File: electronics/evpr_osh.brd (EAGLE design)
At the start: 88.6 x 42.7 mm, 140 parts

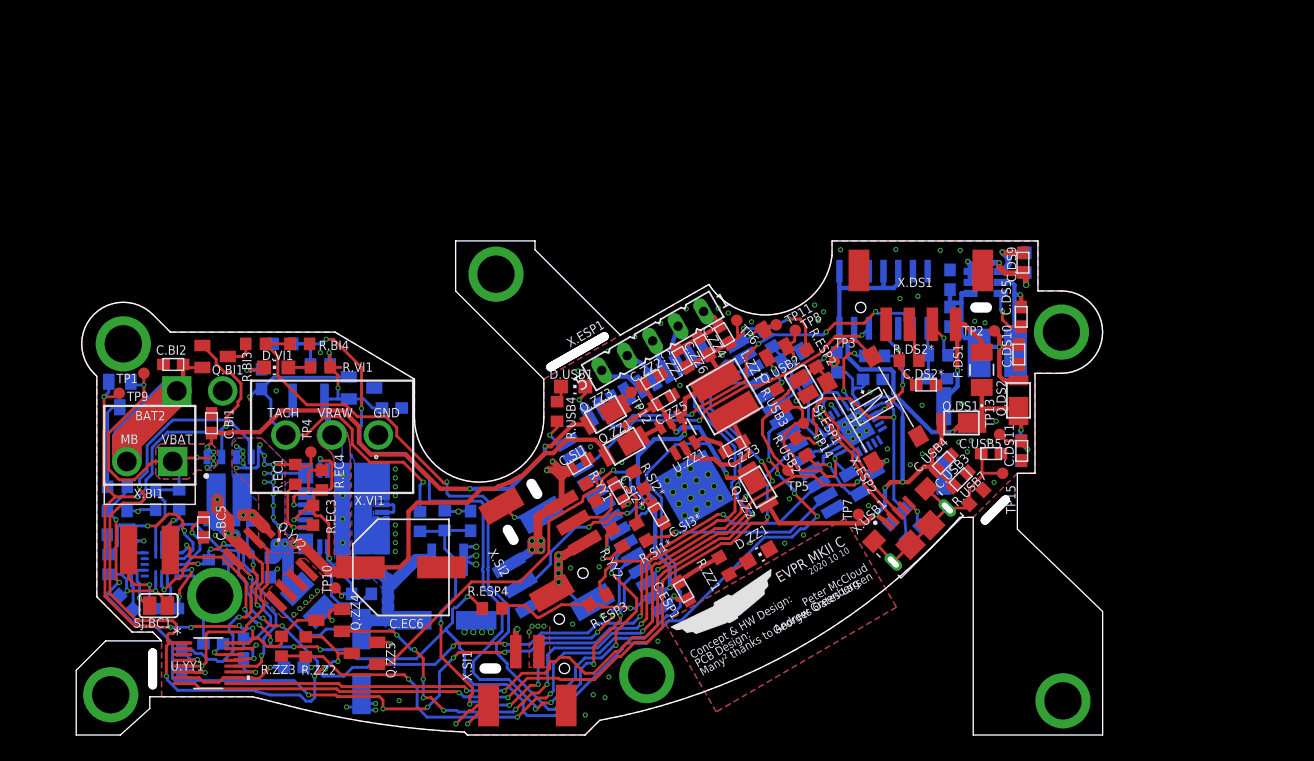
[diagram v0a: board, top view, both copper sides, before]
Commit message: Created OSH version with out-of-board holes removed and shims added. Bumped revision to MKII.D
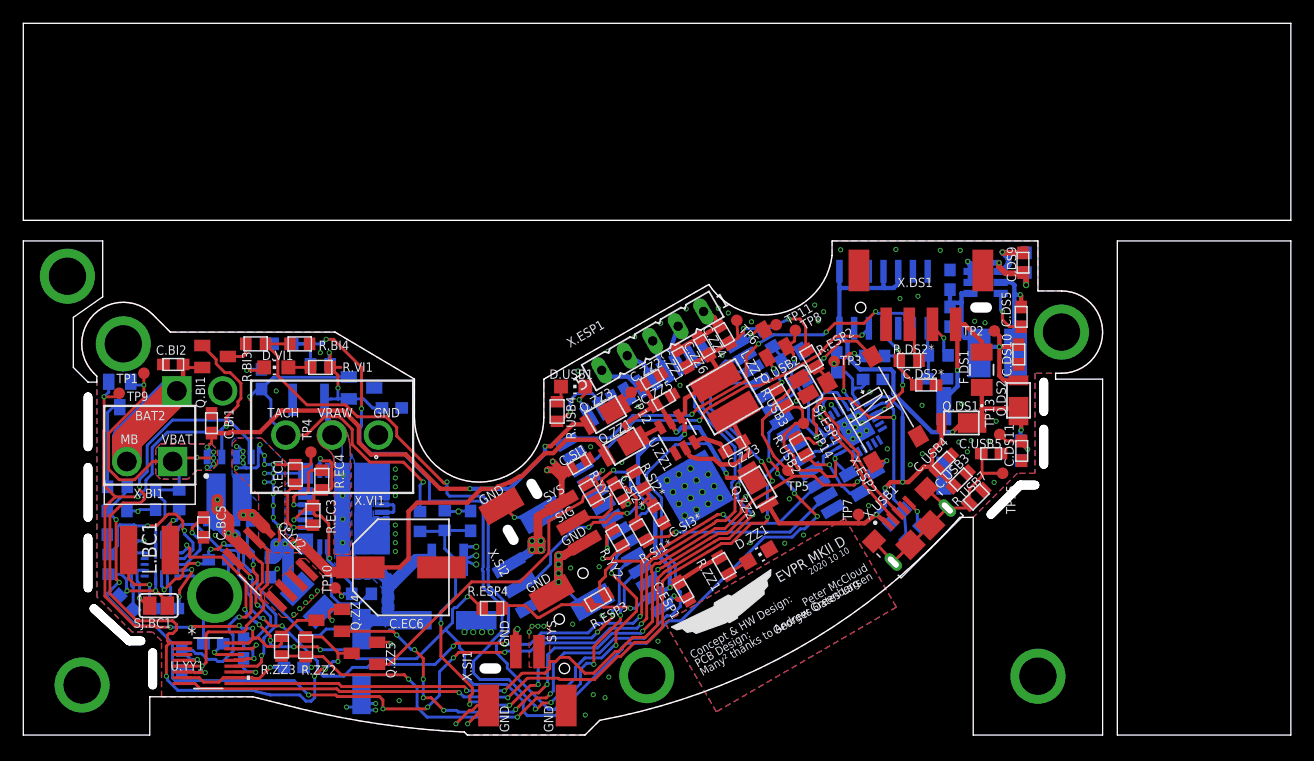
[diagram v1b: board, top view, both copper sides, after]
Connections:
- net USING_ENG renamed !USING_ENG
- new net !USING_BAT: U.ESP1.26
- net DS_CLK: now also U.ESP1.14; no longer U.ESP1.16
- net LED_BUILTIN: now also U.ESP1.16; no longer U.ESP1.14
- net USING_BAT: no longer U.ESP1.26
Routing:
- net LED_BUILTIN: track 3.19 -> 6.28 mm
- net DS_CLK: track 33.5 -> 36.2 mm
- net USING_BAT: track 73.4 -> 72.9 mm
- net GND: vias 124 -> 125
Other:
- board size 88.6 x 42.7 mm -> 109.5 x 61.5 mm
- board text added: "EVPR MKII D"
- board text added: "SIG"
- board text added: "SYS"
- board text removed: "EVPR MKII C"
